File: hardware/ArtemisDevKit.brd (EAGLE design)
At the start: 94 x 38.1 mm, 81 parts, among them J2 CORTEX_JTAG_DEBUG_MINIMUM_PTH, J3 CORTEX_JTAG_DEBUG_PTH, J5 1X04_SMD_STRAIGHT_COMBO, J6 QWIIC_RIGHT_ANGLE, J7 CAMERA-HIMAX, J9 1X04_SMD_STRAIGHT_COMBO, U1 DAPLINK_KL26Z, U2 ARTEMIS_MODULESMD, U3 LIS2DH12, U4 AP2127K-1.8V, X1 16MHz, Y1 32.768kHz

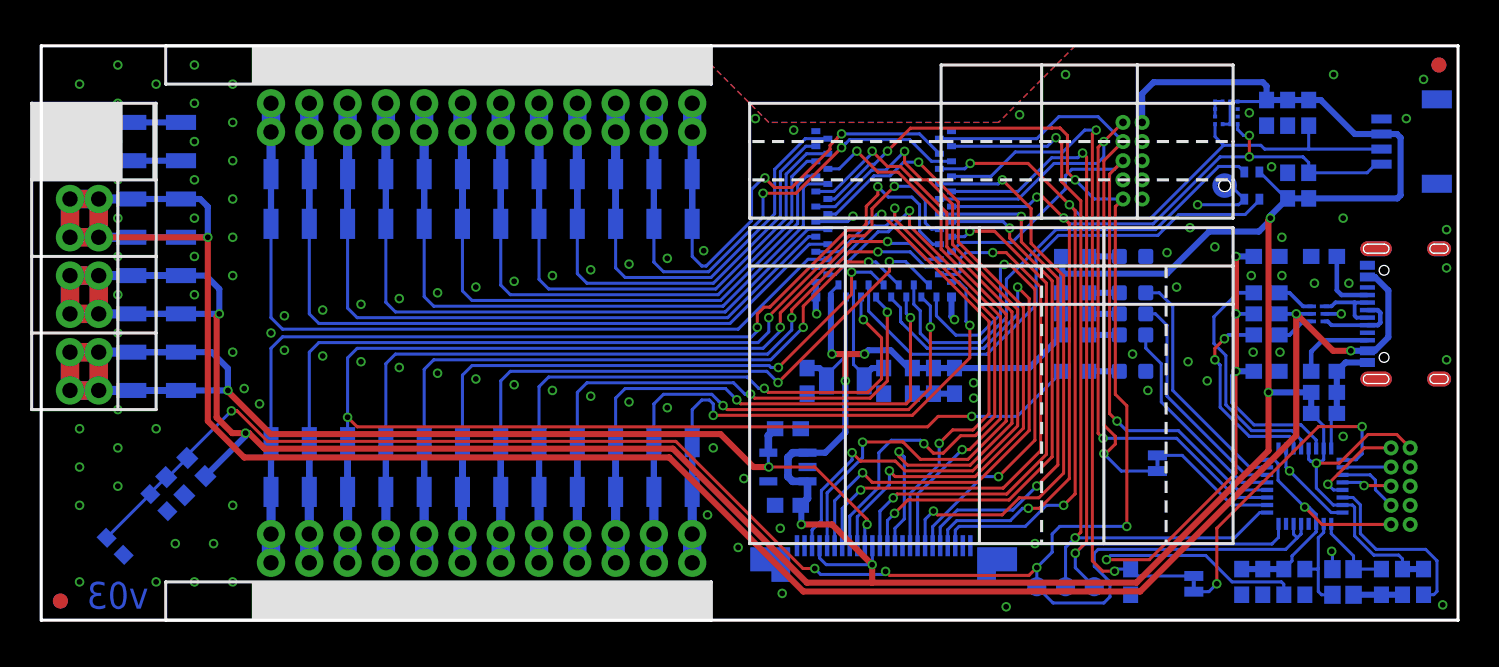
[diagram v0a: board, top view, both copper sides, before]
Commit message: apply changes from proto review
- labeled jumpers w/ matching names and description
- labeled accelerometer axes (bottom)
- increaded power trace widths to 24 mil
- removed VUSB current limiting resistor
- increased buzzard label sizes
- added AP2112K 3.3V regulator (disconnected MKL26Z regulator output from 3.3V bus to avoid contention)
- added product name on top silk
- changed reset button to the tall smd version
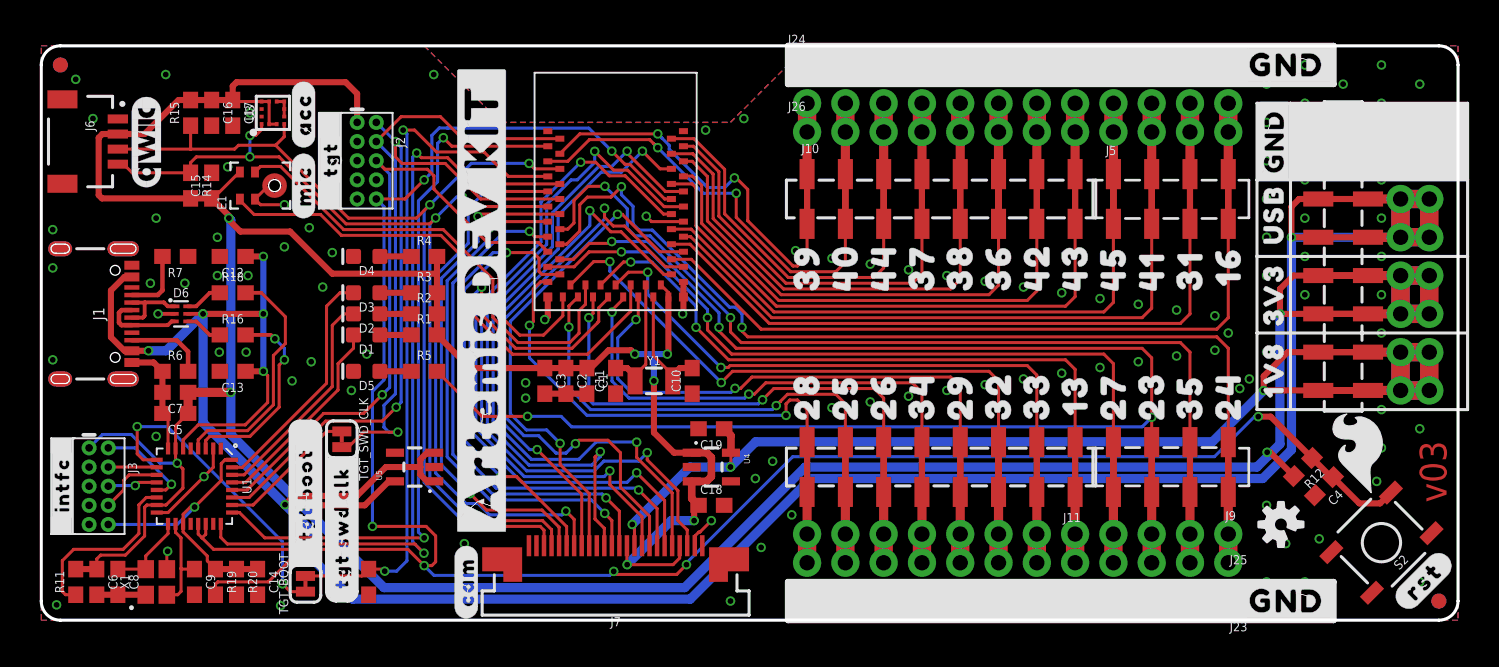
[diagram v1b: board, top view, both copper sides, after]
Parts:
- removed JP1, JP2: JUMPER-SMT_2_NC_TRACE_SILK, SparkFun-Jumpers:SMT-JUMPER_2_NC_TRACE_SILK
- removed R17: 10, SparkFun-Resistors:0603
- removed TP11, TP3, TP4: TEST-POINT3X5, SparkFun-Connectors:PAD.03X.05
- added TGT_BOOT, TGT_SWD_CLK: JUMPER-SMT_2_NC_TRACE_SILK, SparkFun-Jumpers:SMT-JUMPER_2_NC_TRACE_SILK
- added U$1, U$2: (no value), buzzard_labels:#GND#10
- added U$10, U$163, U$55, U$76: (no value), buzzard_labels:55_45
- added U$100, U$29, U$59, U$82, U$88: (no value), buzzard_labels:36_25
- added U$101, U$28, U$60, U$65: (no value), buzzard_labels:37_26
- added U$102, U$152, U$27, U$74: (no value), buzzard_labels:44_34
- added U$103, U$148, U$26, U$63, U$72: (no value), buzzard_labels:40_29
- added U$104, U$150, U$155, U$25: (no value), buzzard_labels:42_32
- added U$105, U$151, U$156, U$24: (no value), buzzard_labels:43_33
- added U$106, U$146, U$23, U$56, U$81: (no value), buzzard_labels:32_13
- added U$107, U$22, U$61, U$71, U$87: (no value), buzzard_labels:38_27
- added U$108, U$21, U$57, U$70: (no value), buzzard_labels:34_23
- added U$109, U$153, U$157, U$20, U$77: (no value), buzzard_labels:45_35
- added U$11, U$161, U$54, U$86, U$91: (no value), buzzard_labels:53_43
- added U$110, U$19, U$58: (no value), buzzard_labels:35_24
- added U$111: (no value), buzzard_labels:1_#ARTEMIS_DEV_KIT#
- added U$112: (no value), buzzard_labels:0_#ARTEMIS_DEV_KIT#
- added U$113: (no value), buzzard_labels:14_A
- added U$114: (no value), buzzard_labels:15_X
- added U$115: (no value), buzzard_labels:16_Y
- added U$116: (no value), buzzard_labels:17_Z
- added U$12, U$160, U$53, U$80, U$90: (no value), buzzard_labels:52_42
- added U$129, U$4: (no value), buzzard_labels:16_1V8
- added U$13, U$52, U$83: (no value), buzzard_labels:46_36
- added U$130, U$5: (no value), buzzard_labels:17_3V3
- added U$131, U$6: (no value), buzzard_labels:18_USB
- added U$132, U$3: (no value), buzzard_labels:15_#GND#
- added U$133: (no value), buzzard_labels:4_#TGT_SWD_CLK#
- added U$134: (no value), buzzard_labels:3_#TGT_BOOT#
- added U$135: (no value), buzzard_labels:1_#INTFC#
- added U$136: (no value), buzzard_labels:2_#TGT#
- added U$137: (no value), buzzard_labels:10_#MIC#
- added U$138: (no value), buzzard_labels:11_#ACC#
- added U$139: (no value), buzzard_labels:12_#CAM#
- added U$14, U$51, U$84, U$92: (no value), buzzard_labels:48_38
- added U$140, U$141: (no value), buzzard_labels:14_#GND#
- added U$142: (no value), buzzard_labels:13_#RST#
- added U$143: (no value), SparkFun-Aesthetics:SFE_LOGO_NAME_FLAME_.2
- added U$145: (no value), buzzard_labels:19_PERIPHERALS
- added U$147, U$64, U$7, U$98: (no value), buzzard_labels:33_16
- added U$149, U$154, U$73, U$8, U$97: (no value), buzzard_labels:41_31
- added U$15, U$158, U$50, U$78: (no value), buzzard_labels:47_37
- added U$159, U$18, U$47, U$67, U$79, U$93: (no value), buzzard_labels:49_39
- added U$16, U$162, U$49, U$69, U$95: (no value), buzzard_labels:54_44
- added U$17, U$48, U$75, U$85, U$94: (no value), buzzard_labels:50_40
- added U$30, U$62, U$66, U$89, U$99: (no value), buzzard_labels:39_28
- added U$31: (no value), buzzard_labels:19_#IOM2#
- added U$33: (no value), buzzard_labels:20_#IOM3#
- added U$34: (no value), buzzard_labels:21_#IOM4#
- added U$35: (no value), buzzard_labels:22_#SCL#SCLK#
- added U$36: (no value), buzzard_labels:23_#SDA#MISO#
- added U$37: (no value), buzzard_labels:24_#MOSI#
- added U$38: (no value), buzzard_labels:30_#PWM#
- added U$39: (no value), buzzard_labels:29_#ADC#
- added U$40: (no value), buzzard_labels:25_#UART0#
- added U$41: (no value), buzzard_labels:26_#UART1#
- added U$42, U$43: (no value), buzzard_labels:27_TX
- added U$44, U$46: (no value), buzzard_labels:28_RX
- added U$68, U$9, U$96: (no value), buzzard_labels:51_41
- added U5: 3.3V, SparkFun-IC-Power:SOT23-5
- S2: device SparkFun-Switches:TACTILE_SWITCH_SMD_4.6X2.8MM -> SparkFun-Switches:TACTILE_SWITCH_SMD_5.2MM
- moved FD1 91.4 mm to (1.27, 36.8), flipped to the top
- moved FD2 91.4 mm to (1.27, 36.8), flipped to the bottom
- moved FD3 91.4 mm to (92.7, 1.27), flipped to the top
- moved FD4 91.4 mm to (92.7, 1.27), flipped to the bottom
- moved J8 90.2 mm to (92.1, 33.0), flipped to the top
- moved R11 89.4 mm to (2.29, 2.54), flipped to the top
- moved C6 86.6 mm to (3.68, 2.54), flipped to the top
- moved J12 86.4 mm to (90.2, 33.0), flipped to the top
- moved J3 86.4 mm to (3.81, 8.89), flipped to the top
- moved C8 83.8 mm to (5.08, 2.54), flipped to the top
- moved J6 83.8 mm to (5.08, 31.8), flipped to the top
- moved S2 82.6 mm to (88.9, 5.14), flipped to the top, turned to 225 degrees
- moved U$45 82.6 mm to (87.6, 11.4), flipped to the top
- moved J1 81.3 mm to (6.35, 20.3), flipped to the top
- moved U$32 80.0 mm to (6.99, 31.8), flipped to the top
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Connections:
- removed net VBUS_IF: D6.5, J1.VBUS1, J1.VBUS2, J12.3, J12.4, J4.3, J4.3@2, J4.4, J4.4@2, J8.3, J8.4, R17.1
- removed net VBUS_IF2: C12.1, C13.1, R17.2, R19.2, U1.6
- new net V_USB: C12.1, C13.1, D6.5, J1.VBUS1, J1.VBUS2, J12.3, J12.4, J4.3, J4.3@2, J4.4, J4.4@2, J8.3, J8.4, R19.2, U1.6, U5.1, U5.3
- net !TGT_RST: no longer S2.4, TP11.P$1
- net 3.3V: now also U5.5; no longer U1.5
- net GND: now also U5.2; no longer S2.2
- net N$12: now also TGT_SWD_CLK.1; no longer JP2.1
- net N$18: now also TGT_BOOT.1; no longer JP1.1
- net TGT_BOOT: now also TGT_BOOT.2; no longer JP1.2
- net TGT_RX: no longer TP4.P$1
- net TGT_SWCLK: now also TGT_SWD_CLK.2; no longer JP2.2
- net TGT_TX: no longer TP3.P$1
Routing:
- net V_USB: track 0.00 -> 196.5 mm, vias 0 -> 8
- net VBUS_IF: track 151.1 -> 0.00 mm, vias 3 -> 0
- net VBUS_IF2: track 51.6 -> 0.00 mm, vias 4 -> 0
- net !TGT_RST: track 151.3 -> 143.6 mm
- net TGT_RX: track 51.5 -> 48.0 mm
- net TGT_TX: track 54.3 -> 51.5 mm
- net 3.3V: track 281.7 -> 284.3 mm, vias 10 -> 11
- net TGT_SWDIO: track 47.4 -> 46.2 mm
- net TGT_SWO: track 44.1 -> 43.1 mm
- net GND: track 111.7 -> 112.7 mm, vias 111 -> 108
- net TGT_SWCLK: track 39.4 -> 38.4 mm
- net N$12: track 8.64 -> 9.30 mm
- net N$18: track 21.1 -> 20.6 mm
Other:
- outline, holes or cut-outs redrawn

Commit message: update to use MKL26Z128VFM4 from SparkFun library
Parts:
- U1: value DAPLINK_KL26Z -> DAPLINK_KL26Z128VFM4; device ArtemisDevKit:QFN-32-NOPAD -> SparkFun-IC-Microcontroller:QFN-32-NOPAD

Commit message: replace sparkfun logo in schematic
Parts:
- removed U$143: (no value), SparkFun-Aesthetics:SFE_LOGO_NAME_FLAME_.2
- added LOGO2: SFE_LOGO_NAME_FLAME.2_INCH, SparkFun-Aesthetics:SFE_LOGO_NAME_FLAME_.2

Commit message: update eagle libs and add LED silk
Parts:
- added U$117: (no value), buzzard_labels:6_PWR
- added U$118: (no value), buzzard_labels:7_COM
- added U$119: (no value), buzzard_labels:8_HID
- added U$120: (no value), buzzard_labels:9_MSD
- added U$121: (no value), buzzard_labels:10_STAT

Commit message: add overbar to reset label
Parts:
- removed U$142: (no value), buzzard_labels:13_#RST#
- added U$122: (no value), buzzard_labels:18_##RST##
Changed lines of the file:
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@@
 <element name="U$140" library="buzzard_labels" package="14_#GND#" value="" x="78.994" y="36.83" smashed="yes"/>
 <element name="U$141" library="buzzard_labels" package="14_#GND#" value="" x="78.994" y="1.27" smashed="yes"/>
-<element name="U$142" library="buzzard_labels" package="13_#RST#" value="" x="90.1065" y="1.016" smashed="yes" rot="R45"/>
 <element name="U$145" library="buzzard_labels" package="19_PERIPHERALS" value="" x="47.3075" y="35.56" smashed="yes" rot="MR0"/>
 <element name="U$7" library="buzzard_labels" package="33_16" value="" x="78.74" y="31.75" smashed="yes" rot="MR270"/>
@@
 <element name="U$120" library="buzzard_labels" package="9_MSD" value="" x="16.002" y="18.923" smashed="yes"/>
 <element name="U$121" library="buzzard_labels" package="10_STAT" value="" x="14.986" y="16.51" smashed="yes"/>
+<element name="U$122" library="buzzard_labels" package="18_##RST##" value="" x="89.8525" y="0.9525" smashed="yes" rot="R45"/>
 </elements>
 <signals>

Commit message: QC double check changes
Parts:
- J1: value (none) -> USB
- J10, J11: value (none) -> SMD
- J14, J22, J23, J24, J25, J26: value (none) -> PTH
- J5, J9: value 1X04_SMD_STRAIGHT_COMBO -> SMD
